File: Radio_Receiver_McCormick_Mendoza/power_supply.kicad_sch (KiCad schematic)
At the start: 0 parts

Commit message: Merge conflict resolution.
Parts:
- added C1: 10uF, symbol Device:C
- added GND, VBAT, VDD, VDDA: TestPoint, TestPoint:TestPoint_Loop_D1.80mm_Drill1.0mm_Beaded, symbol Connector:TestPoint
- added J6: Conn_01x02, Connector_PinHeader_2.54mm:PinHeader_1x02_P2.54mm_Vertical, symbol Connector_Generic:Conn_01x02
- added SW6: 09.03290.01, SWITCH SLIDE SPDT 0.5A 24V 09.03290.01:09.03290_EAO, symbol SWITCH SLIDE SPDT 0.5A 24V 09.03290.01:09.03290.01
- added U2: TPS72748DSER, TPS727-4.8V_regulator:DSE0006A, symbol 2026-04-20_23-44-26:TPS72748DSER
- added U3: TPS72733DSER, TPS727-3.3V_regulator:DSE0006A, symbol TPS72733DSER:TPS72733DSER
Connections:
- new net: C1.1, SW6.3, U2.4 (EN), U2.6 (IN), VBAT.1
- new net: J6.1 (Pin_1), SW6.1
- new net +3.3V: U3.1 (OUT), VDD.1
- new net GND: C1.2, GND.1, J6.2 (Pin_2), U2.2 (NC), U2.3 (GND), U2.5 (NC), U3.2 (NC), U3.3 (GND), U3.5 (NC)
- new net VDDA: U2.1 (OUT), U3.4 (EN), U3.6 (IN), VDDA.1
- no-connect marks 0 -> 1
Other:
- note added: "Battery Input"
- note added: "To Digital parts (RP-2040, etc.)"
- note added: "To the DC Offset and Amplifiers"
- title: (none) -> Radio Receiver

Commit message: Propogated Title Block Fields
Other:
- company: (none) -> Walla Walla University
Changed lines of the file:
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@@
 		(date "2026-04-19")
 		(rev "0.0.1")
+		(company "Walla Walla University")
 		(comment 2 "Daniel Mendoza")
 		(comment 3 "Jeffrey McCormick")

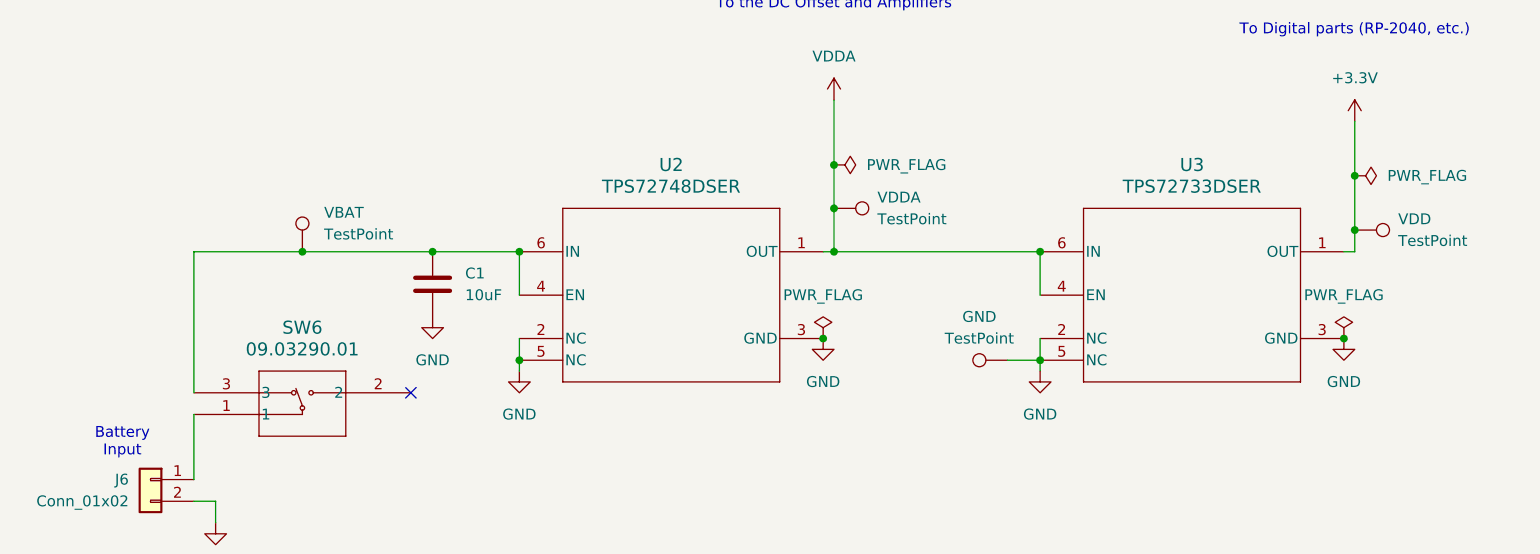
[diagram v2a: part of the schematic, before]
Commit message: Added basic antenna and bandpass filter schematic.
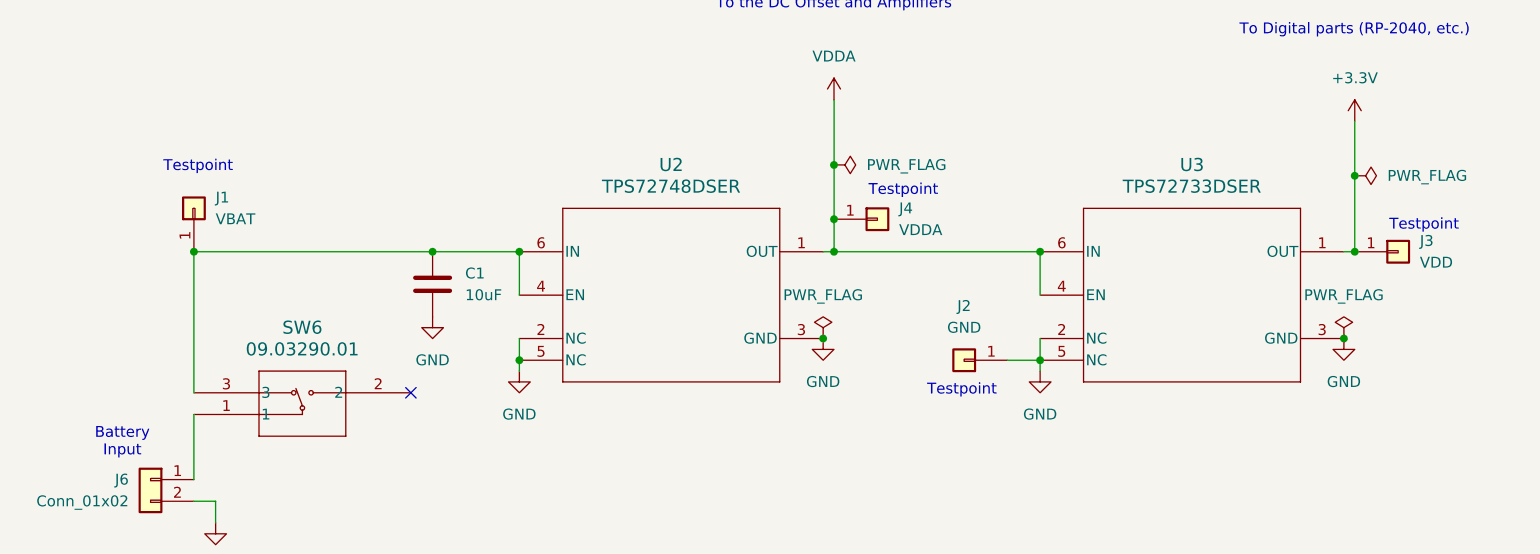
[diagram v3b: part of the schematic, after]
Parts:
- removed GND, VBAT, VDD, VDDA: TestPoint, TestPoint:TestPoint_Loop_D1.80mm_Drill1.0mm_Beaded, symbol Connector:TestPoint
- added J1: VBAT, Connector_PinHeader_2.54mm:PinHeader_1x01_P2.54mm_Vertical, symbol Connector_Generic:Conn_01x01
- added J2: GND, Connector_PinHeader_2.54mm:PinHeader_1x01_P2.54mm_Vertical, symbol Connector_Generic:Conn_01x01
- added J3: VDD, Connector_PinHeader_2.54mm:PinHeader_1x01_P2.54mm_Vertical, symbol Connector_Generic:Conn_01x01
- added J4: VDDA, Connector_PinHeader_2.54mm:PinHeader_1x01_P2.54mm_Vertical, symbol Connector_Generic:Conn_01x01
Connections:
- net +3.3V: now also J3.1 (Pin_1)
- net GND: now also J2.1 (Pin_1)
- net VDDA: now also J4.1 (Pin_1)
- net at C1.1, SW6.3, U2.4 (EN)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: now also J1.1 (Pin_1)
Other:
- note added: "Testpoint"

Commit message: Added Bibliography entry
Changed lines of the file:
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@@
 	(text "To Digital parts (RP-2040, etc.)"
 		(exclude_from_sim no)
-		(at 191.77 75.692 0)
+		(at 191.77 54.102 0)
 		(effects
 			(font
@@
 	)
 	(junction
-		(at 191.77 92.71)
-		(diameter 0)
-		(color 0 0 0 0)
-	)
-	(junction
 		(at 55.88 101.6)
 		(diameter 0)
@@
 	)
 	(junction
+		(at 191.77 92.71)
+		(diameter 0)
+		(color 0 0 0 0)
+	)
+	(junction
 		(at 190.5 111.76)
 		(diameter 0)
@@
 	(wire
 		(pts
-			(xy 191.77 86.36) (xy 191.77 92.71)
+			(xy 191.77 64.77) (xy 191.77 92.71)
 		)
 		(stroke
@@
 	(symbol
 		(lib_id "power:+3.3V")
-		(at 191.77 86.36 0)
+		(at 191.77 64.77 0)
 		(unit 1)
 		(body_style 1)
@@
 		(fields_autoplaced yes)
 		(property "Reference" "#PWR01"
-			(at 191.77 90.17 0)
+			(at 191.77 68.58 0)
 			(hide yes)
 			(show_name no)
@@
 		)
 		(property "Value" "+3.3V"
-			(at 191.77 81.28 0)
+			(at 191.77 59.69 0)
 			(show_name no)
 			(do_not_autoplace no)
@@
 		)
 		(property "Footprint" ""
-			(at 191.77 86.36 0)
+			(at 191.77 64.77 0)
 			(hide yes)
 			(show_name no)
@@
 		)
 		(property "Datasheet" ""
-			(at 191.77 86.36 0)
+			(at 191.77 64.77 0)
 			(hide yes)
 			(show_name no)
@@
 		)
 		(property "Description" "Power symbol creates a global label with name \"+3.3V\""
-			(at 191.77 86.36 0)
-			(hide yes)
-			(show_name no)
+			(at 191.77 64.77 0)
+			(hide yes)
+			(show_name no)

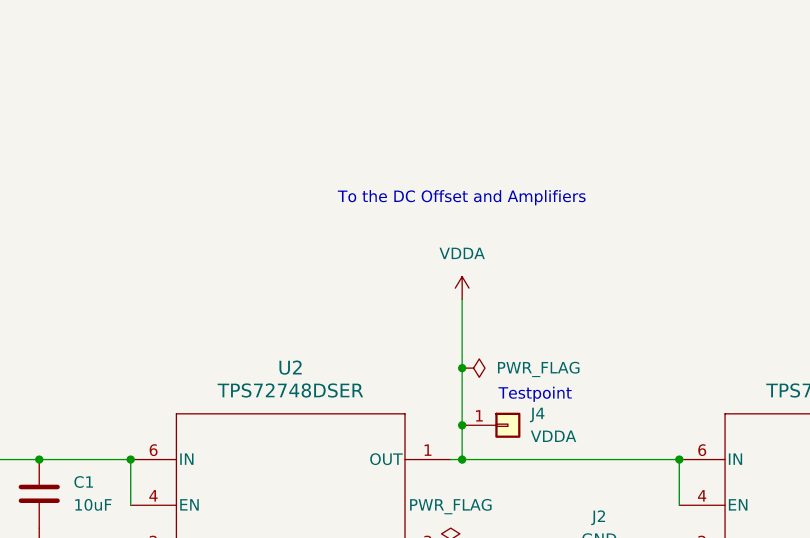
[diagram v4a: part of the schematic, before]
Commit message: Schematic connection edits
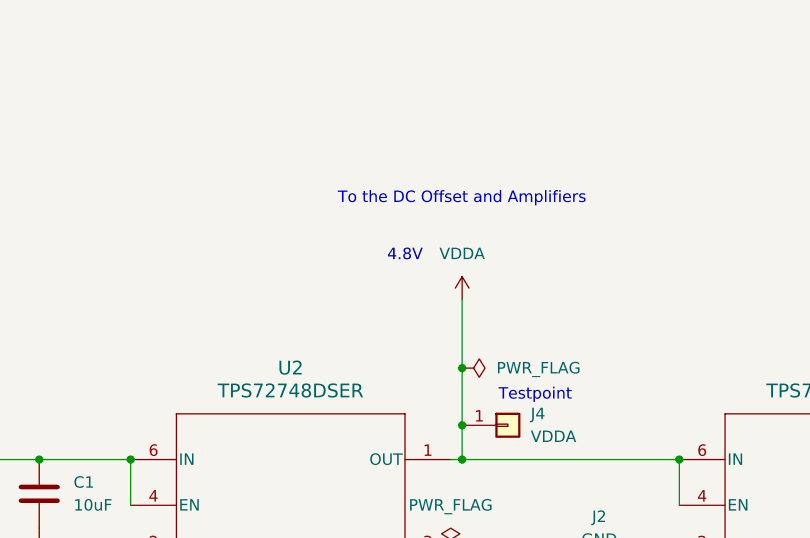
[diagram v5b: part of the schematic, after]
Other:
- note added: "4.8V"
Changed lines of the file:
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@@
 		(comment 3 "Jeffrey McCormick")
+	)
+	(text "4.8V"
+		(exclude_from_sim no)
+		(at 124.46 78.994 0)
+		(effects
+			(font
+				(size 1.27 1.27)
+			)
+		)
 	)
 	(text "Battery\nInput"

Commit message: Schematic edits power and signal systems
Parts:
- added C32, C33, C34, C6: 1uF, PCM_JLCPCB:C_0603, symbol PCM_JLCPCB-Capacitors:0603,1uF
- added FB2, FB3: (no value), PCM_JLCPCB:FB_0603, symbol PCM_JLCPCB-Inductors:Ferrite,0603
- added SW3: SW_SPST, symbol Switch:SW_SPST
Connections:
- net +3.3V: now also FB3.1; no longer J3.1 (Pin_1), U3.1 (OUT)
- net GND: now also C32.2, C33.2, C34.2, C6.2
- net VDDA: now also FB2.1; no longer J4.1 (Pin_1), U2.1 (OUT), U3.4 (EN), U3.6 (IN)
- net at J6.1 (Pin_1): now also SW6.3; no longer SW6.1
- net +5V: now reaches SW6.2
- new net: C32.1, C34.1, FB2.2, J4.1 (Pin_1), U2.1 (OUT), U3.4 (EN), U3.6 (IN)
- new net: C6.1, SW3.2 (B), U2.4 (EN), U2.6 (IN)
- new net: C1.1, J1.1 (Pin_1), SW3.1 (A), SW6.1
- new net: C33.1, FB3.2, J3.1 (Pin_1), U3.1 (OUT)
- no-connect marks 1 -> 0
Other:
- note added: "ON/OFF Switch"
- note added: "USB power"
- moved on the sheet: C1, J1, J3, J6, SW6

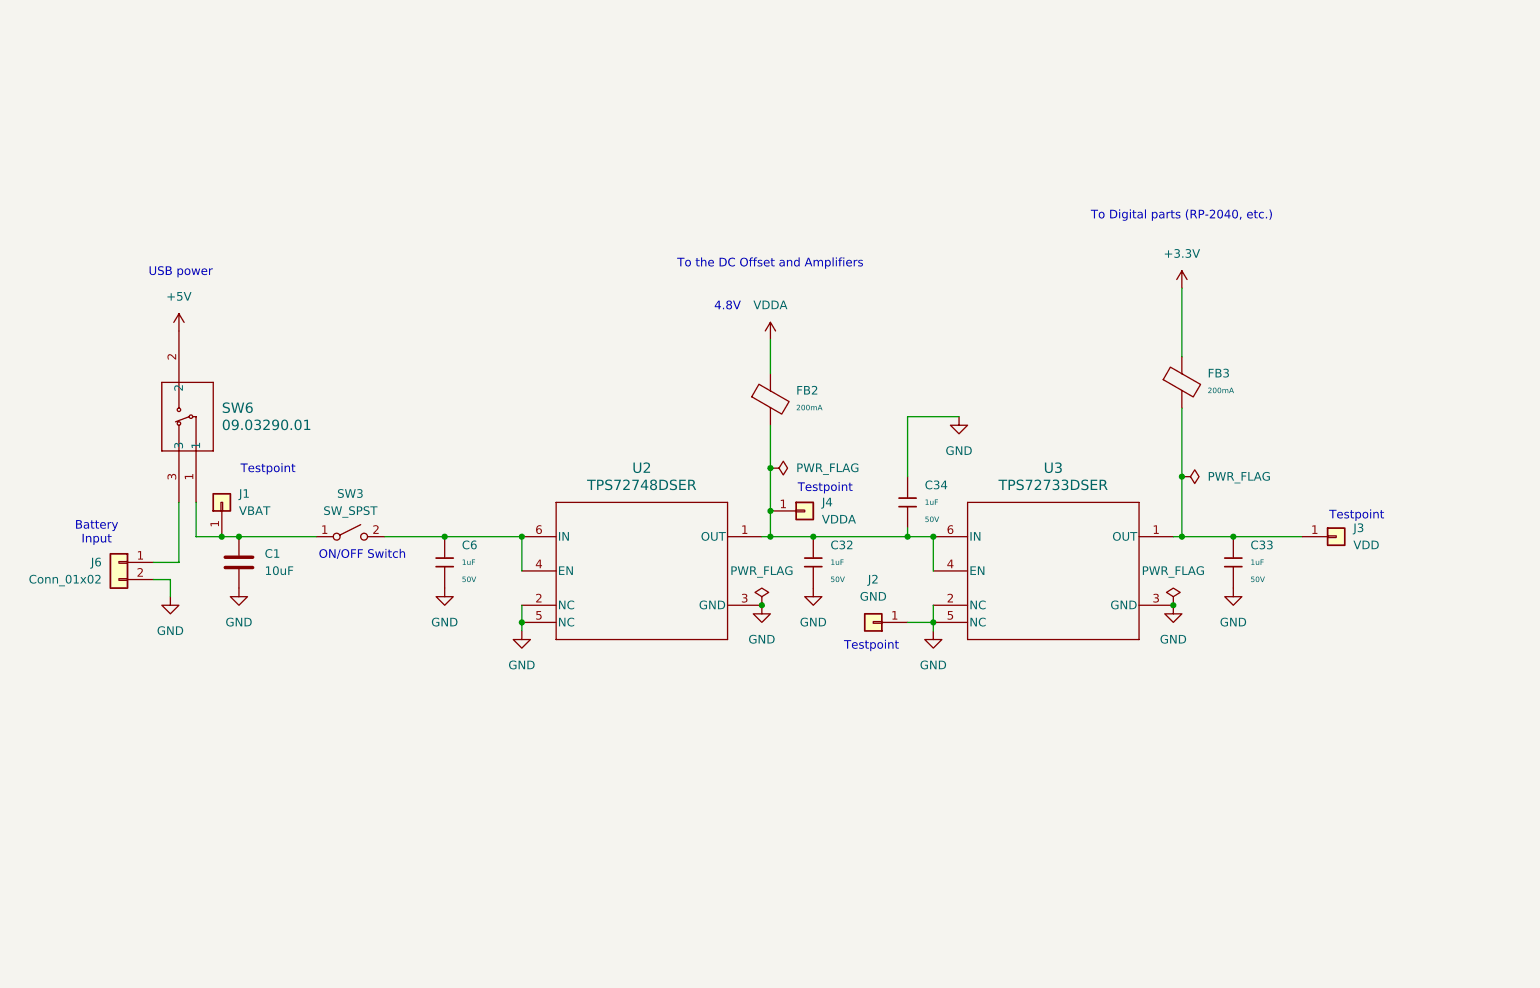
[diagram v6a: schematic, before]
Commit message: Added reference voltage stability by buffer amp
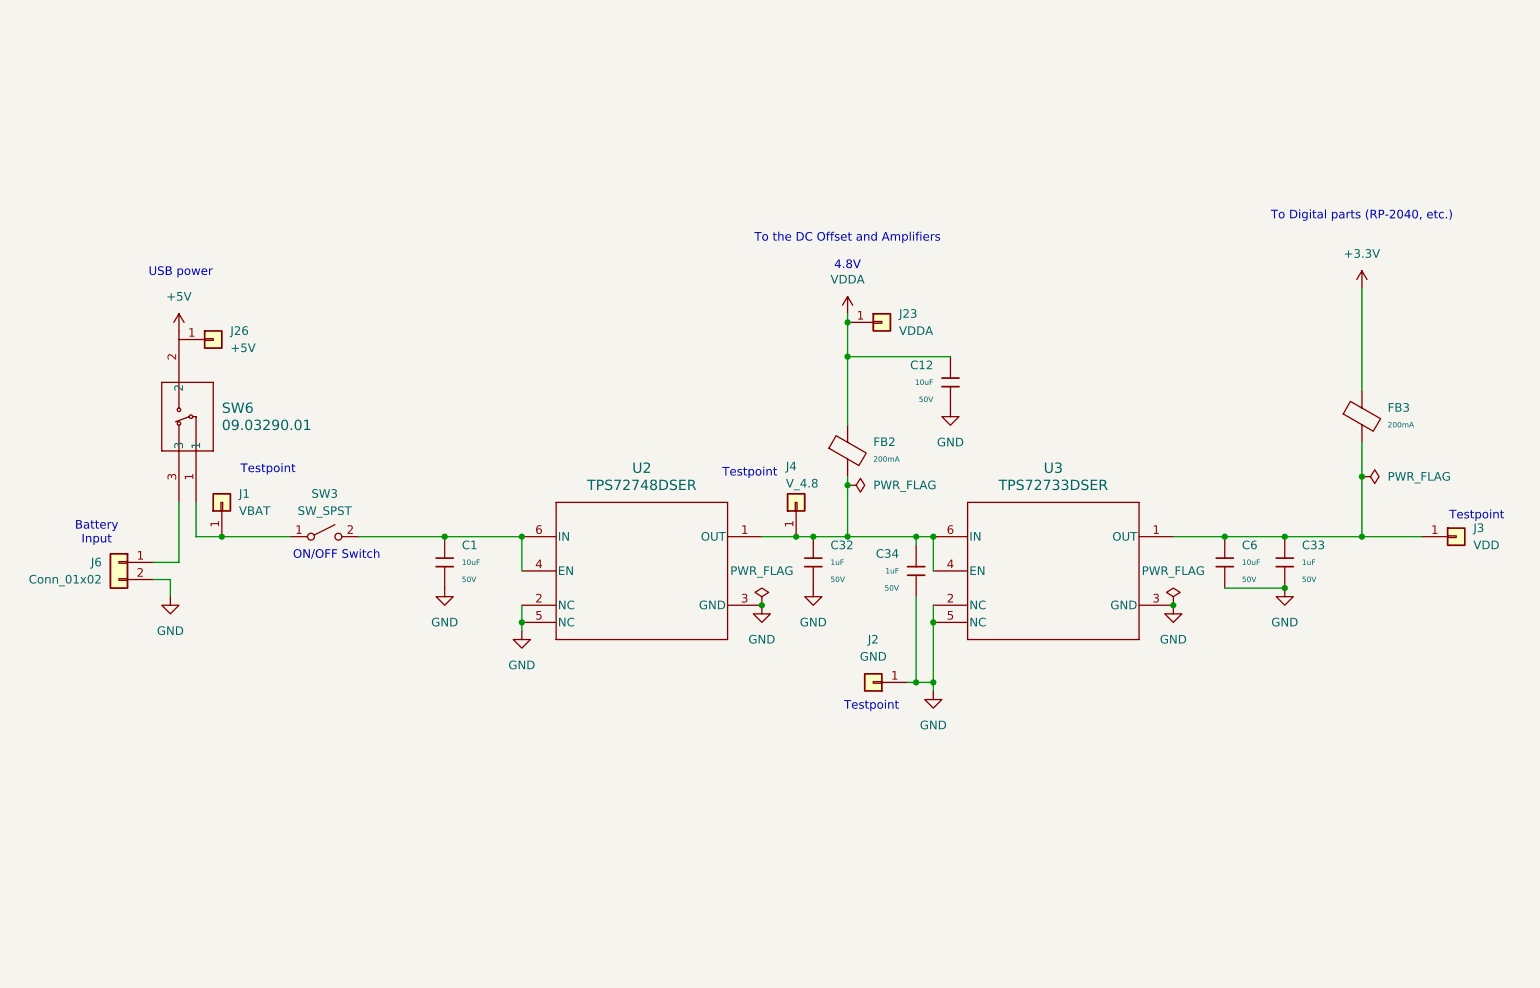
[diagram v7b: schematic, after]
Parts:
- removed C1: 10uF, symbol Device:C
- removed C6: 1uF, PCM_JLCPCB:C_0603, symbol PCM_JLCPCB-Capacitors:0603,1uF
- added C1, C12, C6: 10uF, PCM_JLCPCB:C_0805, symbol PCM_JLCPCB-Capacitors:0805,10uF,(2)
- added J23: VDDA, Connector_PinHeader_2.54mm:PinHeader_1x01_P2.54mm_Vertical, symbol Connector_Generic:Conn_01x01
- added J26: +5V, Connector_PinHeader_2.54mm:PinHeader_1x01_P2.54mm_Vertical, symbol Connector_Generic:Conn_01x01
- J4: value VDDA -> V_4.8
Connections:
- net GND: now also C34.1, C1.2, C12.2, C6.2; no longer C34.2
- net VDDA: now also C12.1, J23.1 (Pin_1)
- net at C32.1, FB2.2, J4.1 (Pin_1)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: now also C34.2; no longer C34.1
- net at SW3.2 (B), U2.4 (EN), U2.6 (IN): now also C1.1
- net at C33.1, FB3.2, J3.1 (Pin_1)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: now also C6.1
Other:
- moved on the sheet: C33, C34, FB2, FB3, J2, J3, J4, SW3

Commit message: Added digital power regulator
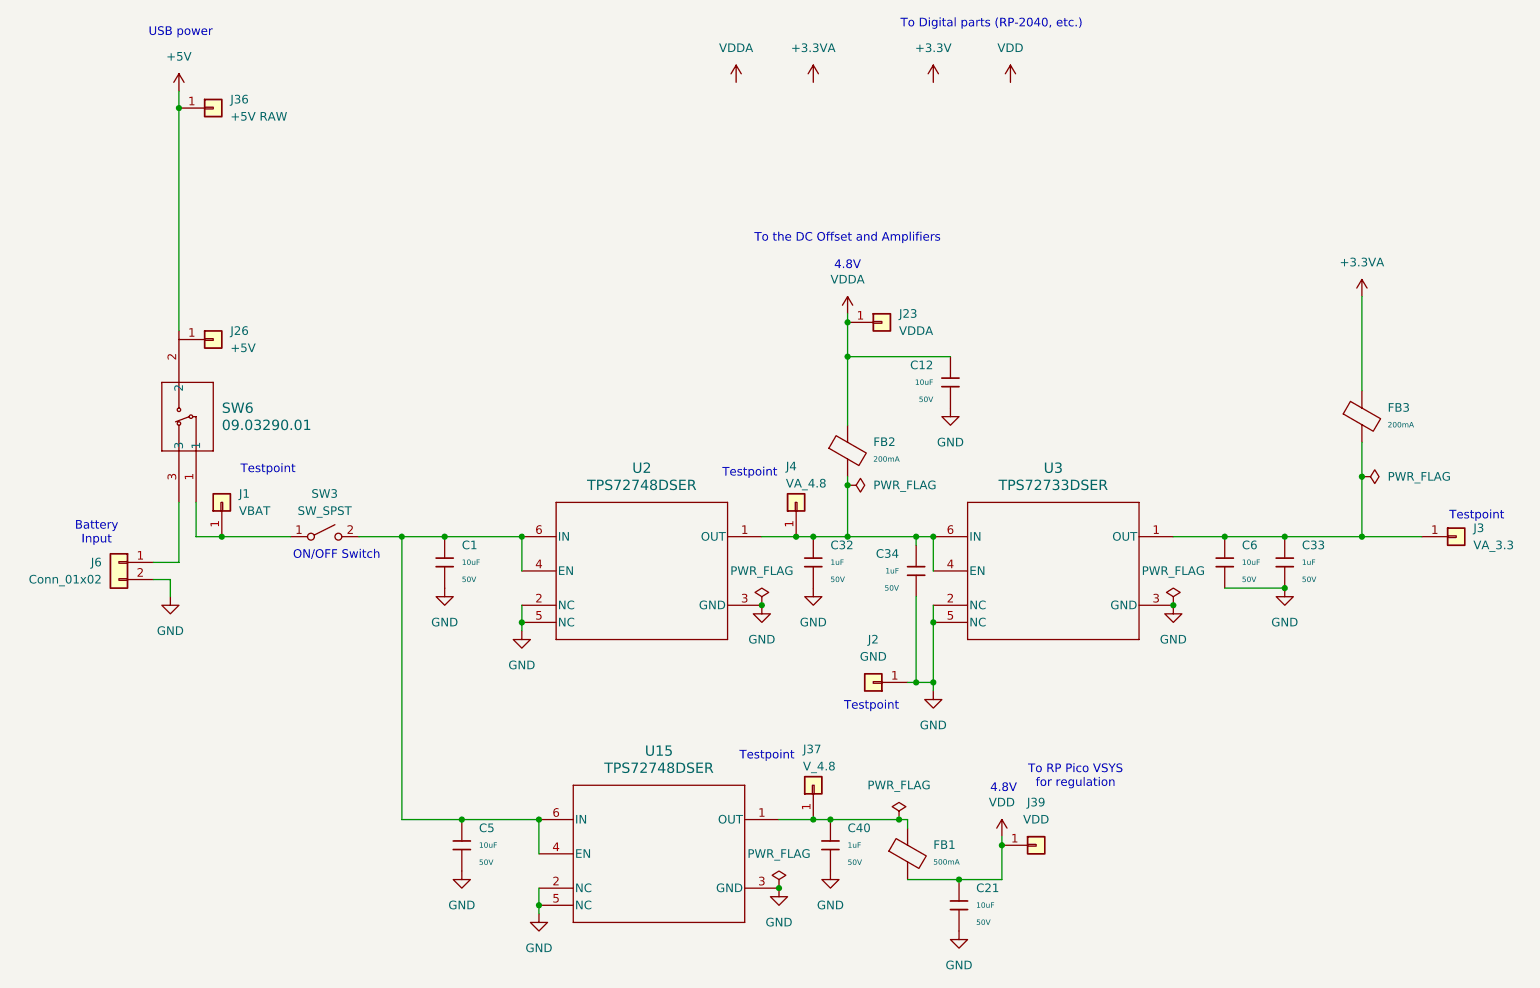
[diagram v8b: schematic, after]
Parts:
- added C21, C5: 10uF, PCM_JLCPCB:C_0805, symbol PCM_JLCPCB-Capacitors:0805,10uF,(2)
- added C40: 1uF, PCM_JLCPCB:C_0603, symbol PCM_JLCPCB-Capacitors:0603,1uF
- added FB1: (no value), PCM_JLCPCB:FB_0805, symbol PCM_JLCPCB-Inductors:Ferrite,0805,(2)
- added J36: +5V RAW, Connector_PinHeader_2.54mm:PinHeader_1x01_P2.54mm_Vertical, symbol Connector_Generic:Conn_01x01
- added J37: V_4.8, Connector_PinHeader_2.54mm:PinHeader_1x01_P2.54mm_Vertical, symbol Connector_Generic:Conn_01x01
- added J39: VDD, Connector_PinHeader_2.54mm:PinHeader_1x01_P2.54mm_Vertical, symbol Connector_Generic:Conn_01x01
- added U15: TPS72748DSER, TPS727-4.8V_regulator:DSE0006A, symbol 2026-04-20_23-44-26:TPS72748DSER
- C1, C12, C6: Manufacturer Murata Electronics -> (none)
- C32, C33, C34: Manufacturer Samsung Electro-Mechanics -> (none)
- FB2, FB3: Manufacturer Sunlord -> (none)
- J3: value VDD -> VA_3.3
- J4: value V_4.8 -> VA_4.8
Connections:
- net +3.3V: no longer FB3.1
- net +5V: now also J36.1 (Pin_1)
- net GND: now also C21.2, C40.2, C5.2, U15.2 (NC), U15.3 (GND), U15.5 (NC)
- net at C1.1, SW3.2 (B), U2.4 (EN)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: now also C5.1, U15.4 (EN), U15.6 (IN)
- new net: C40.1, FB1.1, J37.1 (Pin_1), U15.1 (OUT)
- new net +3.3VA: FB3.1
- new net VDD: C21.1, FB1.2, J39.1 (Pin_1)
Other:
- note added: "To RP Pico VSYS for regulation"
